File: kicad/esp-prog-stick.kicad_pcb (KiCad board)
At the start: 4 copper layers, 15 x 35.5 mm, 15 parts, among them J1 USB_A, J2 JST SM06B-SHLS-TF, Q1 S8050, Q2 S8050, U1 AZ1117-3.3, U2 CH340G, Y1 CSTNE12M0G550000R0

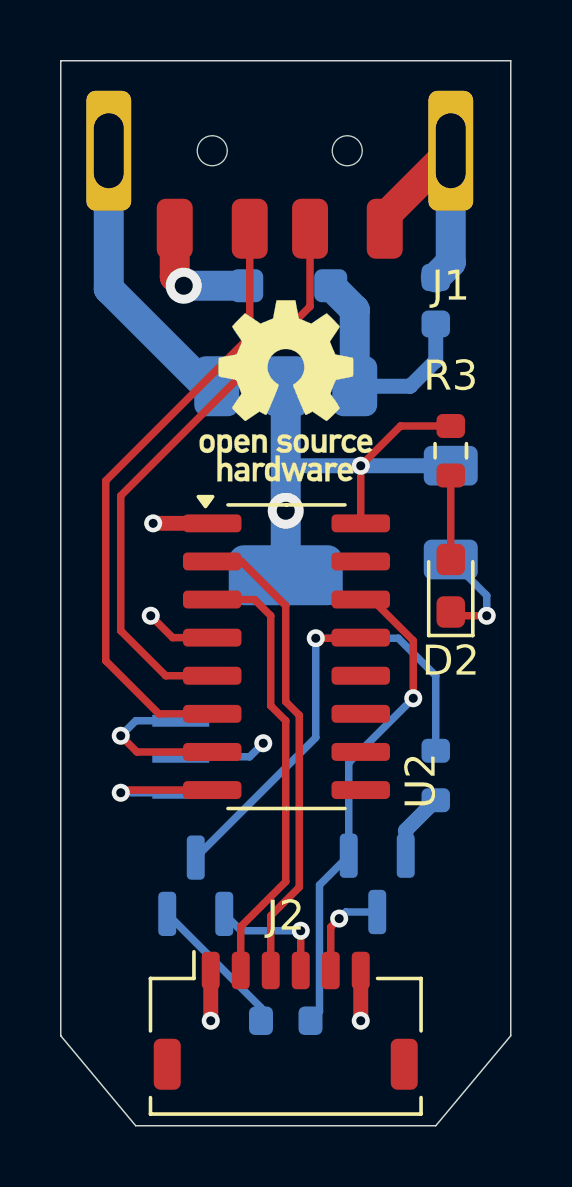
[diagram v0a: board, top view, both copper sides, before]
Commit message: Updated Schematic and BOM File
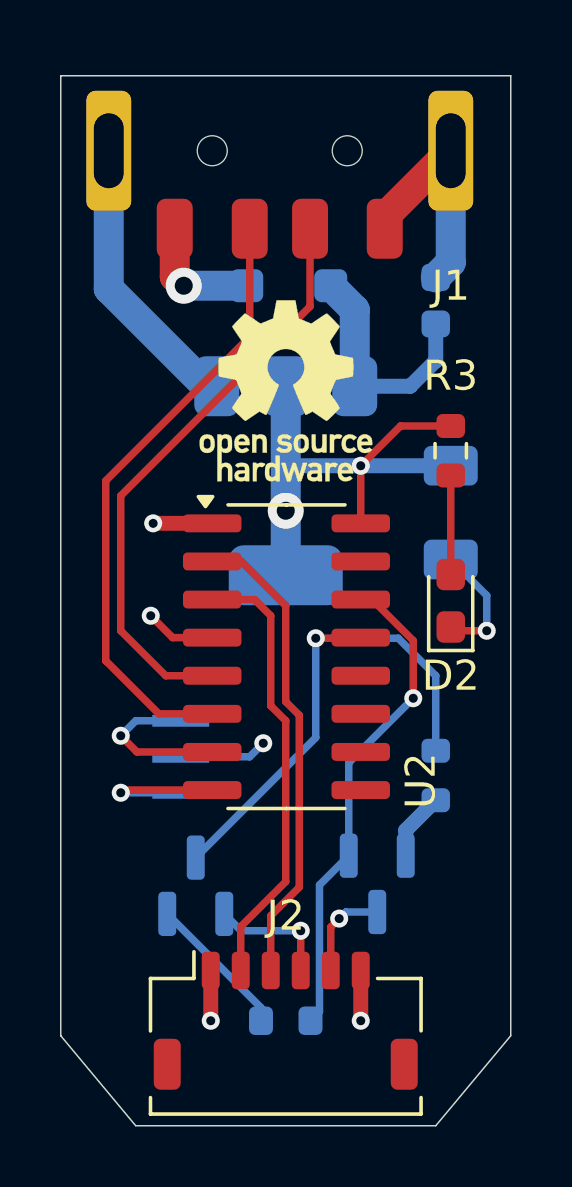
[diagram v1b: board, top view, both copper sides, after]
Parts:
- moved D2 0.50 mm to (205.5, 73.0)
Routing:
- net Net-(D2-A): track 2.80 -> 3.30 mm
- net GND: track 27.7 -> 28.2 mm
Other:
- board size 15 x 35.5 mm -> 15 x 35 mm
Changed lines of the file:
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@@
 			(pintype "passive")
 		)
+		(model "${KICAD8_3DMODEL_DIR}/Connector_USB.3dshapes/USB_A_CNCTech_1001-011-01101_Horizontal.wrl"
+			(offset
+				(xyz 1 9.5 0)
+			)
+			(scale
+				(xyz 1 1 1)
+			)
+			(rotate
+				(xyz 0 0 -90)
+			)
+		)
 	)
 	(footprint "Connector_JST:JST_SHL_SM06B-SHLS-TF_1x06-1MP_P1.00mm_Horizontal"
@@
 			(roundrect_rratio 0.25)
 		)
-		(model "${KICAD8_3DMODEL_DIR}/Connector_JST.3dshapes/JST_SHL_SM06B-SHLS-TF_1x06-1MP_P1.00mm_Horizontal.wrl"
+		(model "/home/harexew/Downloads/SM06B-SHLS-TF.STEP"
 			(offset
-				(xyz 0 0 0)
+				(xyz 0 -0.5 0)
 			)
 			(scale
@@
 			)
 			(rotate
-				(xyz 0 0 0)
+				(xyz -90 0 0)
 			)
 		)
@@
 	(footprint "LED_SMD:LED_0603_1608Metric_Pad1.05x0.95mm_HandSolder"
 		(layer "F.Cu")
-		(at 205.5 72.5 90)
+		(at 205.5 73 90)
 		(descr "LED SMD 0603 (1608 Metric), square (rectangular) end terminal, IPC_7351 nominal, (Body size source: http://www.tortai-tech.com/upload/download/2011102023233369053.pdf), generated with kicad-footprint-generator")
 		(tags "LED handsolder")
@@
 	(gr_poly
 		(pts
-			(xy 192.5 55) (xy 207.5 55) (xy 207.5 87.5) (xy 205 90.5) (xy 195 90.5) (xy 192.5 87.5)
+			(xy 192.5 55.5) (xy 207.5 55.5) (xy 207.5 87.5) (xy 205 90.5) (xy 195 90.5) (xy 192.5 87.5)
 		)
 		(stroke
@@
 		)
 	)
+	(dimension
+		(type orthogonal)
+		(layer "Dwgs.User")
+		(pts
+			(xy 207.5 73) (xy 207.5 55.5)
+		)
+		(height 7.5)
+		(orientation 1)
+		(gr_text "17,5 mm"
+			(at 213.85 64.25 90)
+			(layer "Dwgs.User")
+			(effects
+				(font
+					(size 1 1)
+					(thickness 0.15)
+				)
+			)
+		)
+		(format
+			(prefix "")
+			(suffix "")
+			(units 3)
+			(units_format 1)
+			(precision 4) suppress_zeroes)
+		(style
+			(thickness 0.1)
+			(arrow_length 1.27)
+			(text_position_mode 0)
+			(extension_height 0.58642)
+			(extension_offset 0.5) keep_text_aligned)
+	)
+	(dimension
+		(type orthogonal)
+		(layer "Dwgs.User")
+		(pts
+			(xy 207.5 87.5) (xy 205 90.5)
+		)
+		(height 7)
+		(orientation 1)
+		(gr_text "3 mm"
+			(at 216.5 89 90)
+			(layer "Dwgs.User")
+			(effects
+				(font
+					(size 1 1)
+					(thickness 0.15)
+				)
+			)
+		)
+		(format
+			(prefix "")
+			(suffix "")
+			(units 3)
+			(units_format 1)
+			(precision 4) suppress_zeroes)
+		(style
+			(thickness 0.1)
+			(arrow_length 1.27)
+			(text_position_mode 2)
+			(extension_height 0.58642)
+			(extension_offset 0.5) keep_text_aligned)
+	)
+	(dimension
+		(type orthogonal)
+		(layer "Dwgs.User")
+		(pts
+			(xy 192.5 55.5) (xy 207.5 55.5)
+		)
+		(height -19.5)
+		(orientation 0)
+		(gr_text "15 mm"
+			(at 200 34.85 0)
+			(layer "Dwgs.User")
+			(effects
+				(font
+					(size 1 1)
+					(thickness 0.15)
+				)
+			)
+		)
+		(format
+			(prefix "")
+			(suffix "")
+			(units 3)
+			(units_format 1)
+			(precision 4) suppress_zeroes)
+		(style
+			(thickness 0.1)
+			(arrow_length 1.27)
+			(text_position_mode 0)
+			(extension_height 0.58642)
+			(extension_offset 0.5) keep_text_aligned)
+	)
+	(dimension
+		(type orthogonal)
+		(layer "Dwgs.User")
+		(pts
+			(xy 192.5 55.5) (xy 195.1 90.5)
+		)
+		(height -9)
+		(orientation 1)
+		(gr_text "35 mm"
+			(at 182.35 73 90)
+			(layer "Dwgs.User")
+			(effects
+				(font
+					(size 1 1)
+					(thickness 0.15)
+				)
+			)
+		)
+		(format
+			(prefix "")
+			(suffix "")
+			(units 3)
+			(units_format 1)
+			(precision 4) suppress_zeroes)
+		(style
+			(thickness 0.1)
+			(arrow_length 1.27)
+			(text_position_mode 0)
+			(extension_height 0.58642)
+			(extension_offset 0.5) keep_text_aligned)
+	)
+	(dimension
+		(type orthogonal)
+		(layer "Dwgs.User")
+		(pts
+			(xy 205 90.5) (xy 195 90.5)
+		)
+		(height 6.5)
+		(orientation 0)
+		(gr_text "10 mm"
+			(at 200 95.85 0)
+			(layer "Dwgs.User")
+			(effects
+				(font
+					(size 1 1)
+					(thickness 0.15)
+				)
+			)
+		)
+		(format
+			(prefix "")
+			(suffix "")
+			(units 3)
+			(units_format 1)
+			(precision 4) suppress_zeroes)
+		(style
+			(thickness 0.1)
+			(arrow_length 1.27)
+			(text_position_mode 0)
+			(extension_height 0.58642)
+			(extension_offset 0.5) keep_text_aligned)
+	)
 	(segment
 		(start 195.58 70.42)
@@
 	)
 	(segment
-		(start 205.625 73.5)
-		(end 205.5 73.375)
+		(start 206.7 74)
+		(end 205.625 74)
 		(width 0.25)
 		(layer "F.Cu")
@@
 	)
 	(segment
-		(start 203.3 60.6)
-		(end 203.3 60.2)
-		(width 1)
+		(start 205.625 74)
+		(end 205.5 73.875)
+		(width 0.25)
 		(layer "F.Cu")
 		(net 1)
 	)
 	(segment
-		(start 206.7 73.5)
-		(end 205.625 73.5)
-		(width 0.25)
+		(start 203.3 60.6)
+		(end 203.3 60.2)
+		(width 1)
 		(layer "F.Cu")
 		(net 1)
@@
 	)
 	(via
-		(at 206.7 73.5)
+		(at 206.7 74)
 		(size 0.6)
 		(drill 0.3)
@@
 	)
 	(segment
-		(start 206.7 73.5)
-		(end 206.7 72.825)
-		(width 0.25)
-		(layer "B.Cu")
-		(net 1)
-	)
-	(segment
 		(start 196.5 78.2)
 		(end 198.8 78.2)
@@
 	)
 	(segment
+		(start 206.7 74)
+		(end 206.7 72.825)
+		(width 0.25)
+		(layer "B.Cu")
+		(net 1)
+	)
+	(segment
 		(start 206.7 72.825)
 		(end 205.5 71.625)
@@
 	(segment
 		(start 205.5 68.825)
-		(end 205.5 71.625)
+		(end 205.5 72.125)
 		(width 0.25)
 		(layer "F.Cu")
@@
 		(min_thickness 0.25)
 		(filled_areas_thickness no)
-		(fill yes
+		(fill
 			(thermal_gap 0.5)
 			(thermal_bridge_width 0.5)
@@
 		(polygon
 			(pts
-				(xy 192.5 55) (xy 207.5 55) (xy 207.5 87.5) (xy 205 90.5) (xy 195 90.5) (xy 192.5 87.5)
+				(xy 192.5 55.5) (xy 207.5 55.5) (xy 207.5 87.5) (xy 205 90.5) (xy 195 90.5) (xy 192.5 87.5)
 			)
 		)
@@
 		(min_thickness 0.25)
 		(filled_areas_thickness no)
-		(fill yes
+		(fill
 			(thermal_gap 0.5)
 			(thermal_bridge_width 0.5)
@@
 		(polygon
 			(pts
-				(xy 207.5 55) (xy 192.5 55) (xy 192.5 87.5) (xy 195 90.5) (xy 205 90.5) (xy 207.5 87.5)
+				(xy 207.5 55.5) (xy 192.5 55.5) (xy 192.5 87.5) (xy 195 90.5) (xy 205 90.5) (xy 207.5 87.5)
 			)
 		)
